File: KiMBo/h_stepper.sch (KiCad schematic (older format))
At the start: 24 parts, among them U23 TMC2130

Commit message: Arrange connectors and E-stepper circuit
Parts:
- R179: footprint Resistors_SMD:R_0805 -> Resistors_SMD:R_0603
- R181: footprint Resistors_SMD:R_0603 -> Resistors_SMD:R_0805
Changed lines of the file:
@@
 F 0 "R181" H 10500 7500 50  0000 R CNN
 F 1 "220mΩ" H 10500 7600 50  0000 R CNN
-F 2 "Resistors_SMD:R_0603" V 10480 7550 50  0001 C CNN
+F 2 "Resistors_SMD:R_0805" V 10480 7550 50  0001 C CNN
 F 3 "" H 10550 7550 50  0000 C CNN
 	1    10550 7550
@@
 F 0 "R179" V 9050 7750 50  0000 C CNN
 F 1 "4.75kΩ" V 9150 7750 50  0000 C CNN
-F 2 "Resistors_SMD:R_0805" V 9180 7750 50  0001 C CNN
+F 2 "Resistors_SMD:R_0603" V 9180 7750 50  0001 C CNN
 F 3 "" H 9250 7750 50  0000 C CNN
 	1    9250 7750

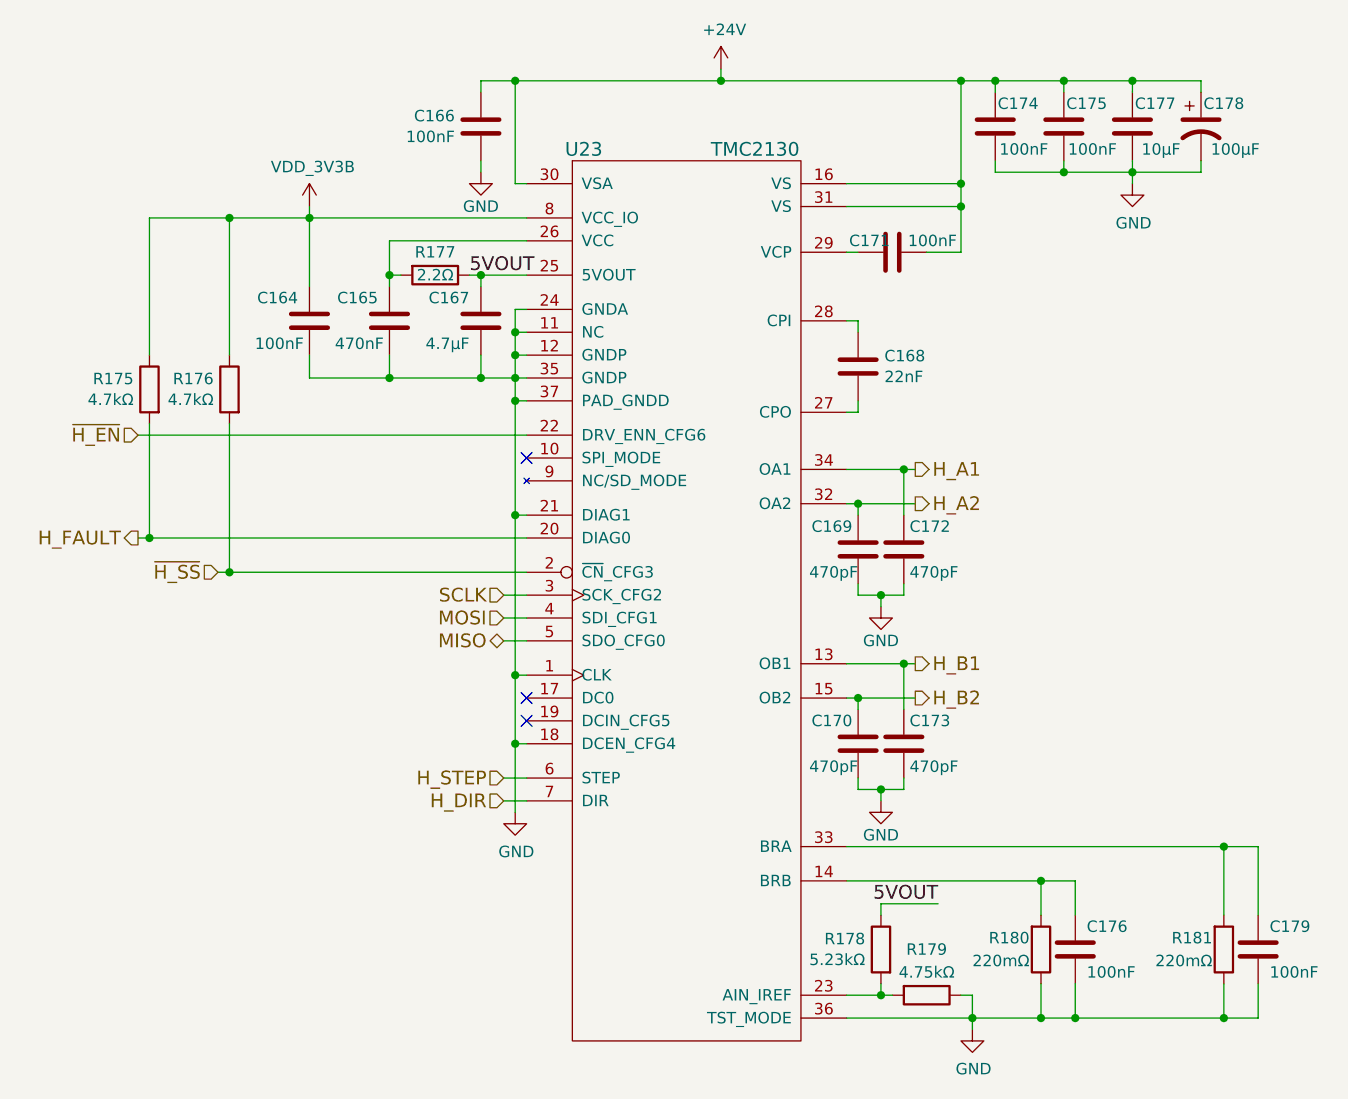
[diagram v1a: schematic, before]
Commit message: Remove HDMI from the schematic
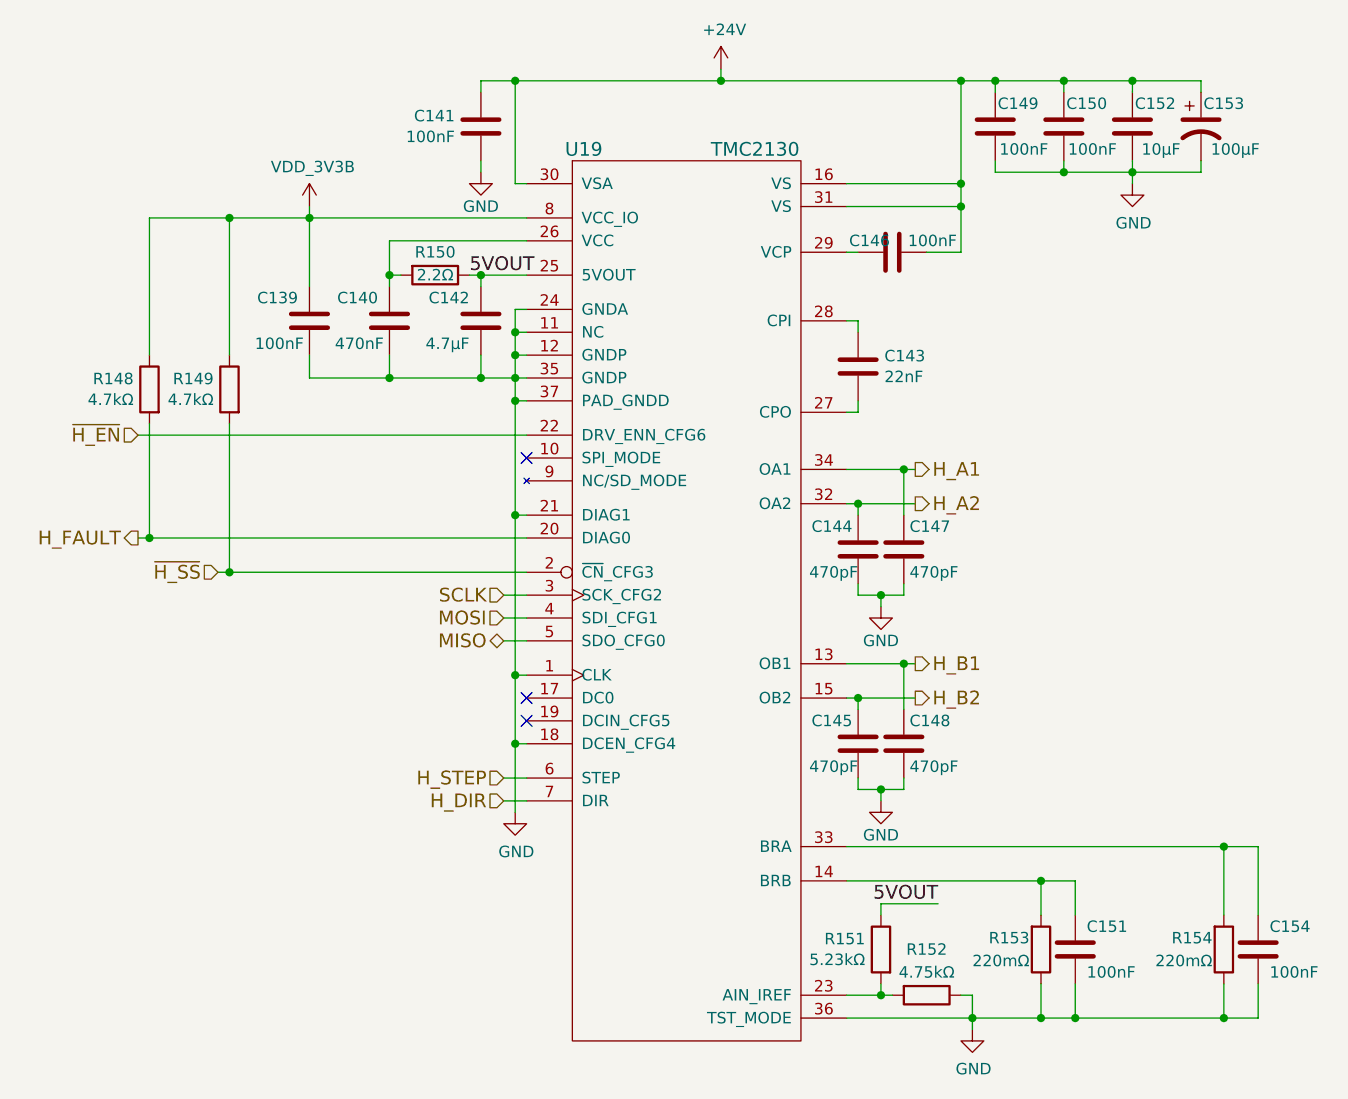
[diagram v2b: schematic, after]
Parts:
- renumbered C164 to C139, C165 to C140, C166 to C141, C167 to C142, C168 to C143, C169 to C144, C170 to C145, C171 to C146, C172 to C147, C173 to C148, C174 to C149, C175 to C150, C176 to C151, C177 to C152, C178 to C153, C179 to C154, R175 to R148, R176 to R149, R177 to R150, R178 to R151, R179 to R152, R180 to R153, R181 to R154, U23 to U19
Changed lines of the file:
@@
 $Descr A3 16535 11693
 encoding utf-8
-Sheet 21 26
+Sheet 21 25
 Title ""
 Date ""
@@
 MOSI
 $Comp
-L C C166
+L C C141
 U 1 1 5BA7E11E
 P 7300 3950
-F 0 "C166" H 7186 3904 50  0000 R CNN
+F 0 "C141" H 7186 3904 50  0000 R CNN
 F 1 "100nF" H 7186 3995 50  0000 R CNN
 F 2 "Capacitors_SMD:C_0603" H 7338 3800 50  0001 C CNN
@@
 $EndComp
 $Comp
-L C C171
+L C C146
 U 1 1 589B8C70
 P 9100 4500
-F 0 "C171" V 9050 4400 50  0000 C CNN
+F 0 "C146" V 9050 4400 50  0000 C CNN
 F 1 "100nF" V 9050 4675 50  0000 C CNN
 F 2 "Capacitors_SMD:C_0603" H 9138 4350 50  0001 C CNN
@@
 $EndComp
 $Comp
-L CP1 C178
+L CP1 C153
 U 1 1 589B8CBD
 P 10450 3950
-F 0 "C178" H 10550 4050 50  0000 C CNN
+F 0 "C153" H 10550 4050 50  0000 C CNN
 F 1 "100μF" H 10600 3850 50  0000 C CNN
 F 2 "Capacitors_SMD:c_elec_8x10" H 10450 3950 50  0001 C CNN
@@
 $EndComp
 $Comp
-L C C174
+L C C149
 U 1 1 5BA7E121
 P 9550 3950
-F 0 "C174" H 9450 4050 50  0000 C CNN
+F 0 "C149" H 9450 4050 50  0000 C CNN
 F 1 "100nF" H 9425 3850 50  0000 C CNN
 F 2 "Capacitors_SMD:C_0603" H 9588 3800 50  0001 C CNN
@@
 $EndComp
 $Comp
-L GND #PWR0240
+L GND #PWR0209
 U 1 1 5BA7E122
 P 7300 4150
-F 0 "#PWR0240" H 7300 3900 50  0001 C CNN
+F 0 "#PWR0209" H 7300 3900 50  0001 C CNN
 F 1 "GND" H 7300 4000 50  0000 C CNN
 F 2 "" H 7300 4150 50  0000 C CNN
@@
 $EndComp
 $Comp
-L C C175
+L C C150
 U 1 1 5BA7E123
 P 9850 3950
-F 0 "C175" H 9750 4050 50  0000 C CNN
+F 0 "C150" H 9750 4050 50  0000 C CNN
 F 1 "100nF" H 9725 3850 50  0000 C CNN
 F 2 "Capacitors_SMD:C_0603" H 9888 3800 50  0001 C CNN
@@
 $EndComp
 $Comp
-L GND #PWR0241
+L GND #PWR0210
 U 1 1 5BA7E124
 P 10150 4200
-F 0 "#PWR0241" H 10150 3950 50  0001 C CNN
+F 0 "#PWR0210" H 10150 3950 50  0001 C CNN
 F 1 "GND" H 10155 4027 50  0000 C CNN
 F 2 "" H 10150 4200 50  0000 C CNN
@@
 $EndComp
 $Comp
-L +24V #PWR0242
+L +24V #PWR0211
 U 1 1 589BEDE1
 P 8350 3700
-F 0 "#PWR0242" H 8350 3550 50  0001 C CNN
+F 0 "#PWR0211" H 8350 3550 50  0001 C CNN
 F 1 "+24V" H 8365 3873 50  0000 C CNN
 F 2 "" H 8350 3700 50  0000 C CNN
@@
 $EndComp
 $Comp
-L C C168
+L C C143
 U 1 1 5BA7E126
 P 8950 5000
-F 0 "C168" H 9065 5046 50  0000 L CNN
+F 0 "C143" H 9065 5046 50  0000 L CNN
 F 1 "22nF" H 9065 4955 50  0000 L CNN
 F 2 "Capacitors_SMD:C_0603" H 8988 4850 50  0001 C CNN
@@
 $EndComp
 $Comp
-L R R181
+L R R154
 U 1 1 5BA7E127
 P 10550 7550
-F 0 "R181" H 10500 7500 50  0000 R CNN
+F 0 "R154" H 10500 7500 50  0000 R CNN
 F 1 "220mΩ" H 10500 7600 50  0000 R CNN
 F 2 "Resistors_SMD:R_0805" V 10480 7550 50  0001 C CNN
@@
 $EndComp
 $Comp
-L R R180
+L R R153
 U 1 1 5BA7E128
 P 9750 7550
-F 0 "R180" H 9700 7500 50  0000 R CNN
+F 0 "R153" H 9700 7500 50  0000 R CNN
 F 1 "220mΩ" H 9700 7600 50  0000 R CNN
 F 2 "Resistors_SMD:R_0805" V 9680 7550 50  0001 C CNN
@@
 $EndComp
 $Comp
-L GND #PWR0243
+L GND #PWR0212
 U 1 1 589C2B70
 P 9450 7900
-F 0 "#PWR0243" H 9450 7650 50  0001 C CNN
+F 0 "#PWR0212" H 9450 7650 50  0001 C CNN
 F 1 "GND" H 9455 7727 50  0000 C CNN
 F 2 "" H 9450 7900 50  0000 C CNN
@@
 NoConn ~ 7500 6450
 $Comp
-L R R177
+L R R150
 U 1 1 589C4ED8
 P 7100 4600
-F 0 "R177" V 7000 4600 50  0000 C CNN
+F 0 "R150" V 7000 4600 50  0000 C CNN
 F 1 "2.2Ω" V 7100 4600 50  0000 C CNN
 F 2 "Resistors_SMD:R_0603" V 7030 4600 50  0001 C CNN
@@
 $EndComp
 $Comp
-L C C165
+L C C140
 U 1 1 5BA7E12C
 P 6900 4800
-F 0 "C165" H 6950 4900 50  0000 L CNN
+F 0 "C140" H 6950 4900 50  0000 L CNN
 F 1 "470nF" H 6925 4700 50  0000 L CNN
 F 2 "Capacitors_SMD:C_0603" H 6938 4650 50  0001 C CNN
@@
 NoConn ~ 7500 6550
 $Comp
-L GND #PWR0244
+L GND #PWR0213
 U 1 1 5BA7E12D
 P 7450 6950
-F 0 "#PWR0244" H 7450 6700 50  0001 C CNN
+F 0 "#PWR0213" H 7450 6700 50  0001 C CNN
 F 1 "GND" H 7455 6777 50  0000 C CNN
 F 2 "" H 7450 6950 50  0000 C CNN
@@
 $EndComp
 $Comp
-L C C176
+L C C151
 U 1 1 589CC9B9
 P 9900 7550
-F 0 "C176" H 9950 7650 50  0000 L CNN
+F 0 "C151" H 9950 7650 50  0000 L CNN
 F 1 "100nF" H 9950 7450 50  0000 L CNN
 F 2 "Capacitors_SMD:C_0603" H 9938 7400 50  0001 C CNN
@@
 H_FAULT
 $Comp
-L R R175
+L R R148
 U 1 1 5BA7E12F
 P 5850 5100
-F 0 "R175" H 5919 5146 50  0000 L CNN
+F 0 "R148" H 5919 5146 50  0000 L CNN
 F 1 "4.7kΩ" H 5919 5055 50  0000 L CNN
 F 2 "Resistors_SMD:R_0603" V 5780 5100 50  0001 C CNN
@@
 NoConn ~ 7500 5400
 $Comp
-L C C167
+L C C142
 U 1 1 589C396E
 P 7300 4800
-F 0 "C167" H 7350 4900 50  0000 L CNN
+F 0 "C142" H 7350 4900 50  0000 L CNN
 F 1 "4.7μF" H 7350 4700 50  0000 L CNN
 F 2 "Capacitors_SMD:C_0603" H 7338 4650 50  0001 C CNN
@@
 5VOUT
 $Comp
-L R R178
+L R R151
 U 1 1 5BA7E130
 P 9050 7550
-F 0 "R178" H 9119 7596 50  0000 L CNN
+F 0 "R151" H 9119 7596 50  0000 L CNN
 F 1 "5.23kΩ" H 9119 7505 50  0000 L CNN
 F 2 "Resistors_SMD:R_0603" V 8980 7550 50  0001 C CNN
@@
 5VOUT
 $Comp
-L R R179
+L R R152
 U 1 1 5BA7E131
 P 9250 7750
-F 0 "R179" V 9050 7750 50  0000 C CNN
+F 0 "R152" V 9050 7750 50  0000 C CNN
 F 1 "4.75kΩ" V 9150 7750 50  0000 C CNN
 F 2 "Resistors_SMD:R_0603" V 9180 7750 50  0001 C CNN
@@
 $EndComp
 $Comp
-L R R176
+L R R149
 U 1 1 58A47723
 P 6200 5100
-F 0 "R176" H 6269 5146 50  0000 L CNN
+F 0 "R149" H 6269 5146 50  0000 L CNN
 F 1 "4.7kΩ" H 6269 5055 50  0000 L CNN
 F 2 "Resistors_SMD:R_0603" V 6130 5100 50  0001 C CNN
@@
 $EndComp
 $Comp
-L C C179
+L C C154
 U 1 1 58AF169E
 P 10700 7550
-F 0 "C179" H 10750 7650 50  0000 L CNN
+F 0 "C154" H 10750 7650 50  0000 L CNN
 F 1 "100nF" H 10750 7450 50  0000 L CNN
 F 2 "Capacitors_SMD:C_0603" H 10738 7400 50  0001 C CNN
@@
 $EndComp
 $Comp
-L C C169
+L C C144
 U 1 1 58B19CCF
 P 8950 5800
-F 0 "C169" H 8975 5900 50  0000 L CNN
+F 0 "C144" H 8975 5900 50  0000 L CNN
 F 1 "470pF" H 8950 5700 50  0000 L CNN
 F 2 "Capacitors_SMD:C_0603" H 8988 5650 50  0001 C CNN
@@
 $EndComp
 $Comp
-L GND #PWR0245
+L GND #PWR0214
 U 1 1 5BA7E135
 P 9050 6050
-F 0 "#PWR0245" H 9050 5800 50  0001 C CNN
+F 0 "#PWR0214" H 9050 5800 50  0001 C CNN
 F 1 "GND" H 9050 5900 50  0000 C CNN
 F 2 "" H 9050 6050 50  0000 C CNN
@@
 $EndComp
 $Comp
-L C C172
+L C C147
 U 1 1 5BA7E136
 P 9150 5800
-F 0 "C172" H 9175 5900 50  0000 L CNN
+F 0 "C147" H 9175 5900 50  0000 L CNN
 F 1 "470pF" H 9175 5700 50  0000 L CNN
 F 2 "Capacitors_SMD:C_0603" H 9188 5650 50  0001 C CNN
@@
 $EndComp
 $Comp
-L C C170
+L C C145
 U 1 1 5BA7E137
 P 8950 6650
-F 0 "C170" H 8975 6750 50  0000 L CNN
+F 0 "C145" H 8975 6750 50  0000 L CNN
 F 1 "470pF" H 8950 6550 50  0000 L CNN
 F 2 "Capacitors_SMD:C_0603" H 8988 6500 50  0001 C CNN
@@
 $EndComp
 $Comp
-L GND #PWR0246
+L GND #PWR0215
 U 1 1 5BA7E138
 P 9050 6900
-F 0 "#PWR0246" H 9050 6650 50  0001 C CNN
+F 0 "#PWR0215" H 9050 6650 50  0001 C CNN
 F 1 "GND" H 9050 6750 50  0000 C CNN
 F 2 "" H 9050 6900 50  0000 C CNN
@@
 $EndComp
 $Comp
-L C C173
+L C C148
 U 1 1 5BA7E139
 P 9150 6650
-F 0 "C173" H 9175 6750 50  0000 L CNN
+F 0 "C148" H 9175 6750 50  0000 L CNN
 F 1 "470pF" H 9175 6550 50  0000 L CNN
 F 2 "Capacitors_SMD:C_0603" H 9188 6500 50  0001 C CNN
@@
 $EndComp
 $Comp
-L TMC2130 U23
+L TMC2130 U19
 U 1 1 589A7425
 P 8200 5550
-F 0 "U23" H 7750 7050 60  0000 C CNN
+F 0 "U19" H 7750 7050 60  0000 C CNN
 F 1 "TMC2130" H 8500 7050 60  0000 C CNN
 F 2 "KiMBo:QFN36_5X6" H 8200 5850 60  0001 C CNN
@@
 	8950 6850 8950 6800
 $Comp
-L C C177
+L C C152
 U 1 1 5BA7E13A
 P 10150 3950
-F 0 "C177" H 10050 4050 50  0000 C CNN
+F 0 "C152" H 10050 4050 50  0000 C CNN
 F 1 "10μF" H 10025 3850 50  0000 C CNN
 F 2 "Capacitors_SMD:C_0805" H 10188 3800 50  0001 C CNN
@@
 	5850 4350 7500 4350
 $Comp
-L VDD_3V3B #PWR0247
+L VDD_3V3B #PWR0216
 U 1 1 5A2FEA7A
 P 6550 4300
-F 0 "#PWR0247" H 6550 4150 50  0001 C CNN
+F 0 "#PWR0216" H 6550 4150 50  0001 C CNN
 F 1 "VDD_3V3B" H 6565 4473 50  0000 C CNN
 F 2 "" H 6550 4300 50  0000 C CNN
@@
 $EndComp
 $Comp
-L C C164
+L C C139
 U 1 1 5A897FB1
 P 6550 4800
-F 0 "C164" H 6600 4900 50  0000 L CNN
+F 0 "C139" H 6600 4900 50  0000 L CNN
 F 1 "100nF" H 6575 4700 50  0000 L CNN
 F 2 "Capacitors_SMD:C_0603" H 6588 4650 50  0001 C CNN

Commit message: More stepper motor driver progress
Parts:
- renumbered R148 to R150, R149 to R151, R150 to R152, R151 to R153, R152 to R154, R153 to R155, R154 to R156
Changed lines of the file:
@@
 $Descr A3 16535 11693
 encoding utf-8
-Sheet 21 25
+Sheet 19 25
 Title ""
 Date ""
@@
 $EndComp
 $Comp
-L R R154
+L R R156
 U 1 1 5BA7E127
 P 10550 7550
-F 0 "R154" H 10500 7500 50  0000 R CNN
+F 0 "R156" H 10500 7500 50  0000 R CNN
 F 1 "220mΩ" H 10500 7600 50  0000 R CNN
 F 2 "Resistors_SMD:R_0805" V 10480 7550 50  0001 C CNN
@@
 $EndComp
 $Comp
-L R R153
+L R R155
 U 1 1 5BA7E128
 P 9750 7550
-F 0 "R153" H 9700 7500 50  0000 R CNN
+F 0 "R155" H 9700 7500 50  0000 R CNN
 F 1 "220mΩ" H 9700 7600 50  0000 R CNN
 F 2 "Resistors_SMD:R_0805" V 9680 7550 50  0001 C CNN
@@
 NoConn ~ 7500 6450
 $Comp
-L R R150
+L R R152
 U 1 1 589C4ED8
 P 7100 4600
-F 0 "R150" V 7000 4600 50  0000 C CNN
+F 0 "R152" V 7000 4600 50  0000 C CNN
 F 1 "2.2Ω" V 7100 4600 50  0000 C CNN
 F 2 "Resistors_SMD:R_0603" V 7030 4600 50  0001 C CNN
@@
 H_FAULT
 $Comp
-L R R148
+L R R150
 U 1 1 5BA7E12F
 P 5850 5100
-F 0 "R148" H 5919 5146 50  0000 L CNN
+F 0 "R150" H 5919 5146 50  0000 L CNN
 F 1 "4.7kΩ" H 5919 5055 50  0000 L CNN
 F 2 "Resistors_SMD:R_0603" V 5780 5100 50  0001 C CNN
@@
 5VOUT
 $Comp
-L R R151
+L R R153
 U 1 1 5BA7E130
 P 9050 7550
-F 0 "R151" H 9119 7596 50  0000 L CNN
+F 0 "R153" H 9119 7596 50  0000 L CNN
 F 1 "5.23kΩ" H 9119 7505 50  0000 L CNN
 F 2 "Resistors_SMD:R_0603" V 8980 7550 50  0001 C CNN
@@
 5VOUT
 $Comp
-L R R152
+L R R154
 U 1 1 5BA7E131
 P 9250 7750
-F 0 "R152" V 9050 7750 50  0000 C CNN
+F 0 "R154" V 9050 7750 50  0000 C CNN
 F 1 "4.75kΩ" V 9150 7750 50  0000 C CNN
 F 2 "Resistors_SMD:R_0603" V 9180 7750 50  0001 C CNN
@@
 $EndComp
 $Comp
-L R R149
+L R R151
 U 1 1 58A47723
 P 6200 5100
-F 0 "R149" H 6269 5146 50  0000 L CNN
+F 0 "R151" H 6269 5146 50  0000 L CNN
 F 1 "4.7kΩ" H 6269 5055 50  0000 L CNN
 F 2 "Resistors_SMD:R_0603" V 6130 5100 50  0001 C CNN
